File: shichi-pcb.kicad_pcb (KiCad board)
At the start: 2 copper layers, 266 x 96 mm, 168 parts, among them J1 USB_C_Receptacle_HRO_TYPE-C-3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, J2 Conn_01x04_Male, J3 Conn_01x06_Male, J4 Conn_01x04_Male, J5 Conn_01x01_Male, J6 Conn_01x01_Male, J7 Conn_01x01_Male, K1 SW_Push, K10 SW_Push, K11 SW_Push, K12 SW_Push, K13 SW_Push, K14 SW_Push, K15 SW_Push, K16 SW_Push, K17 SW_Push, K18 SW_Push, K19 SW_Push, K2 SW_Push, K20 SW_Push, K21 SW_Push, K22 SW_Push, K23 SW_Push, K24 SW_Push, K25 SW_Push, K26 SW_Push, K27 SW_Push, K28 SW_Push, K29 SW_Push, K3 SW_Push, K30 SW_Push, K31 SW_Push, K32 SW_Push, K33 SW_Push, K34 SW_Push, K35 SW_Push, K36 SW_Push, K37 SW_Push, K38 SW_Push, K39 SW_Push, K4 SW_Push, K40 SW_Push, K41 SW_Push, K42 SW_Push, K43 SW_Push, K44 SW_Push, K45 SW_Push, K46 SW_Push, K47 SW_Push, K48 SW_Push, K49 SW_Push, K5 SW_Push, K50 SW_Push, K51 SW_Push, K52 SW_Push, K53 SW_Push, K54 SW_Push, K55 SW_Push, K56 SW_Push, K57 SW_Push, K58 SW_Push, K59 SW_Push, K6 SW_Push, K60 SW_Push, K61 SW_Push, K62 SW_Push, K63 SW_Push, K64 SW_Push, K65 SW_Push, K66 SW_Push, K67 SW_Push, K68 SW_Push, K69 SW_Push, K7 SW_Push, K70 SW_Push, K71 SW_Push, K72 SW_Push, K8 SW_Push, K9 SW_Push, SW1 SW_Push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

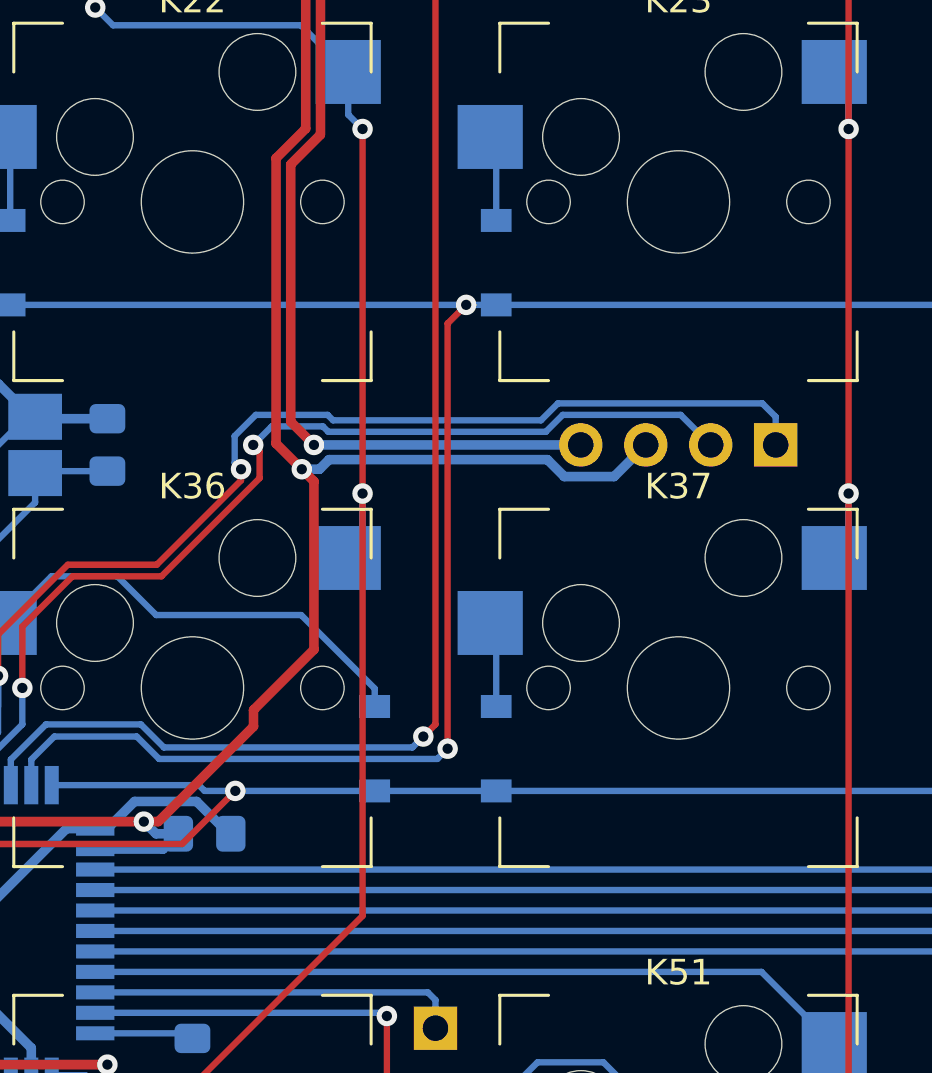
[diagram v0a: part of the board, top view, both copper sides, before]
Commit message: Add polyfuse to PCB layout design
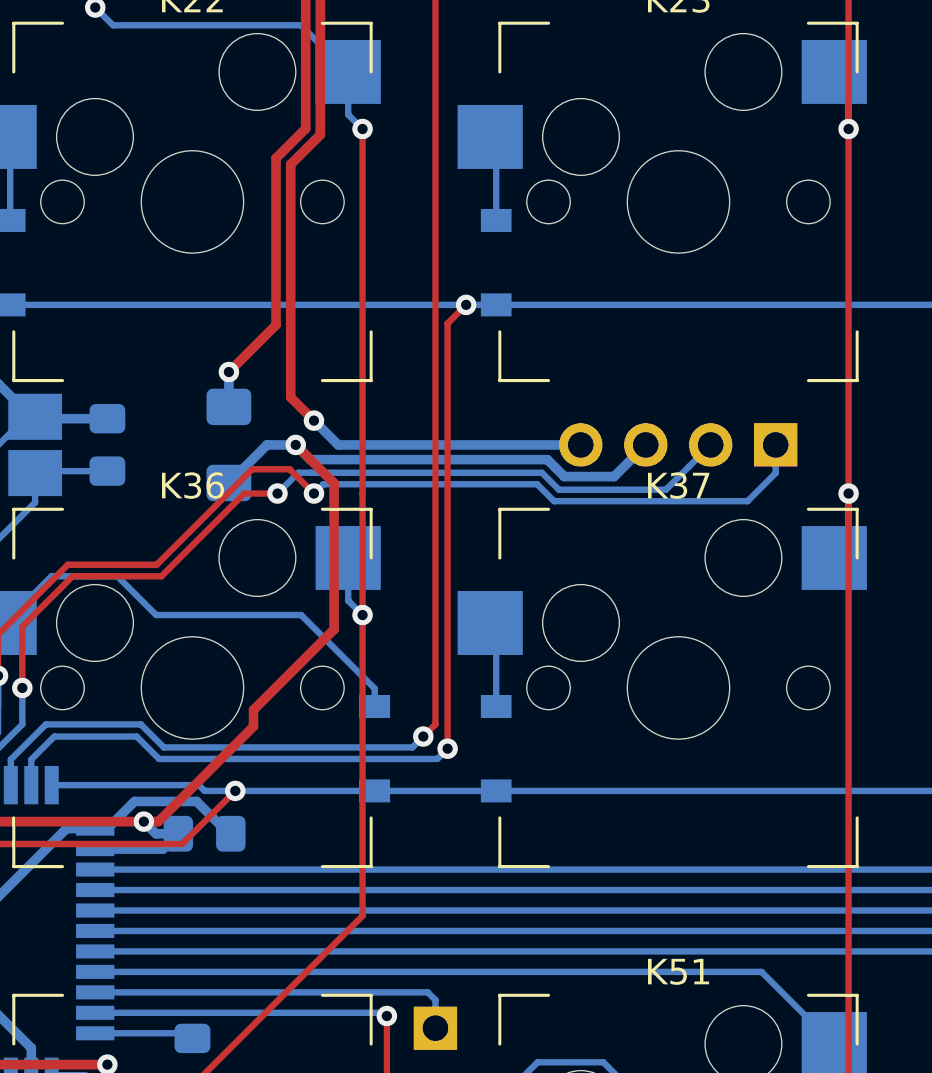
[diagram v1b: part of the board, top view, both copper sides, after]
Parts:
- added F1: Polyfuse, Fuse:Fuse_1206_3216Metric_Pad1.42x1.75mm_HandSolder, B.Cu at (193.9, 88.0)
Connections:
- C3 pad 1: VCC -> +5V
- C5 pad 1: VCC -> +5V
- C6 pad 1: VCC -> +5V
- C7 pad 1: VCC -> +5V
- C8 pad 1: VCC -> +5V
- C9 pad 1: VCC -> +5V
- J3 pad 2: VCC -> +5V
- J4 pad 3: VCC -> +5V
- R5 pad 1: VCC -> +5V
- U2 pad 14: VCC -> +5V
- U2 pad 2: VCC -> +5V
- U2 pad 24: VCC -> +5V
- U2 pad 34: VCC -> +5V
- U2 pad 44: VCC -> +5V
- U2 pad 7: VCC -> +5V
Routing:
- net +5V: track 0.00 -> 147.9 mm, vias 0 -> 8
- net VCC: track 210.7 -> 66.0 mm, vias 11 -> 4
- net SDA: track 38.8 -> 37.1 mm
- net SCL: track 44.6 -> 43.0 mm
- net GND: track 295.1 -> 294.5 mm
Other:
- board text added: "5V"

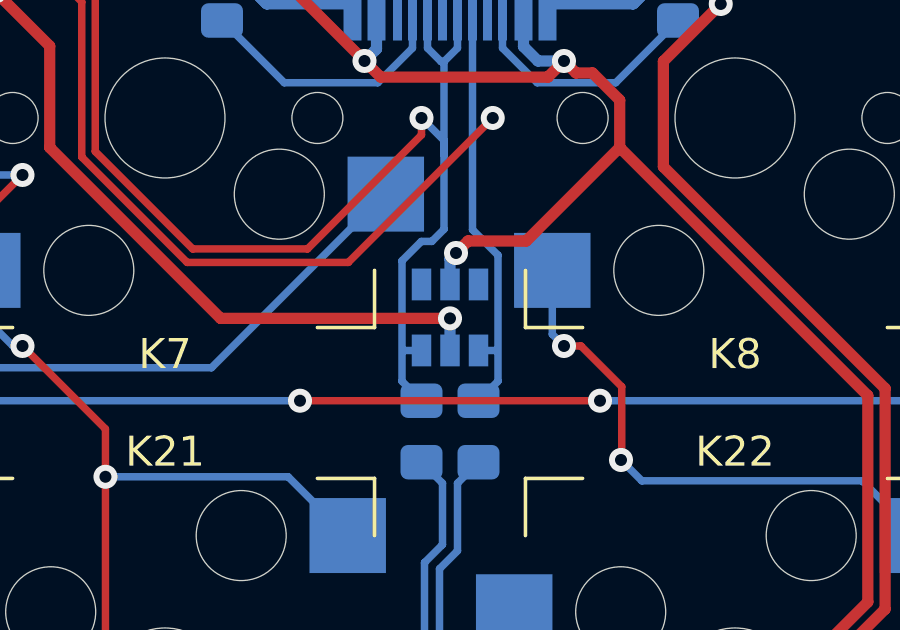
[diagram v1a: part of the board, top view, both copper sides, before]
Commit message: Update PCB layout tracks for ESD Protection
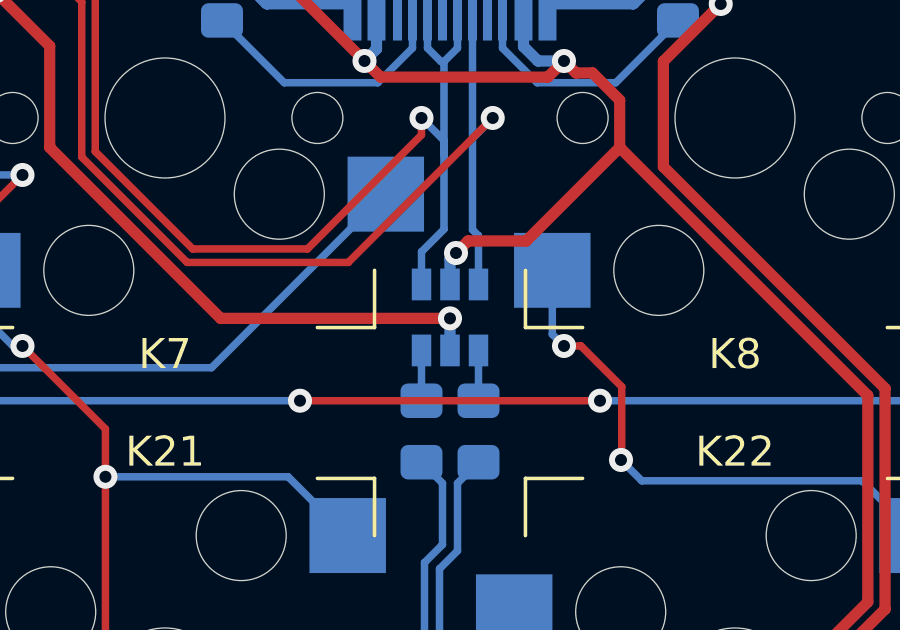
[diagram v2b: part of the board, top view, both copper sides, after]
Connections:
- J1 pad A6: Net-(J1-PadA6) -> D+Bus
- J1 pad A7: Net-(J1-PadA7) -> D-Bus
- J1 pad B6: Net-(J1-PadA6) -> D+Bus
- J1 pad B7: Net-(J1-PadA7) -> D-Bus
- J2 pad 2: Net-(J1-PadA7) -> D-Bus
- J2 pad 3: Net-(J1-PadA6) -> D+Bus
- R3 pad 1: Net-(J1-PadA7) -> Net-(R3-Pad1)
- R4 pad 1: Net-(J1-PadA6) -> Net-(R4-Pad1)
- U1 pad 1: Net-(J1-PadA6) -> Net-(R4-Pad1)
- U1 pad 3: Net-(J1-PadA7) -> Net-(R3-Pad1)
- U1 pad 4: Net-(U1-Pad4) -> D-Bus
- U1 pad 6: Net-(U1-Pad6) -> D+Bus
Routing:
- net Net-(J1-PadA6): track 47.9 -> 0.00 mm, vias 1 -> 0
- net Net-(J1-PadA7): track 43.3 -> 0.00 mm, vias 1 -> 0
- net D+Bus: track 0.00 -> 42.9 mm, vias 0 -> 1
- net D-Bus: track 0.00 -> 38.0 mm, vias 0 -> 1
- net Net-(R4-Pad1): track 0.00 -> 1.67 mm
- net Net-(R3-Pad1): track 0.00 -> 1.67 mm

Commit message: Initial arm PCB layout design
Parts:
- removed the C4 at (171.6, 106.5)
- removed J7: Conn_01x01_Male, Connector_PinHeader_2.54mm:PinHeader_1x01_P2.54mm_Vertical
- removed the R3 at (182.1, 70.0)
- removed R6: 10k, Resistor_SMD:R_0805_2012Metric_Pad1.15x1.40mm_HandSolder
- removed the U2 at (183.0, 107.0)
- removed Y1: Crystal_GND24, Crystal:Crystal_SMD_SeikoEpson_FA238-4Pin_3.2x2.5mm_HandSoldering
- added BZ1: Buzzer, Buzzer_Beeper:Buzzer_Murata_PKMCS0909E4000-R1, B.Cu at (183.0, 123.6)
- added C6: 4.7uF, Capacitor_SMD:C_0805_2012Metric_Pad1.15x1.40mm_HandSolder, B.Cu at (197.5, 88.0)
- added R5: 1k, Resistor_SMD:R_0805_2012Metric_Pad1.15x1.40mm_HandSolder, B.Cu at (175.9, 123.6)
- added SW2: SW_Push, Button_Switch_SMD:SW_SPST_TL3342, B.Cu at (201.1, 52.9)
- added U1: MCP1700-3302E_SOT23, Package_TO_SOT_SMD:SOT-23, B.Cu at (192.5, 88.0)
- added U3: STM32F072CBTx, Package_QFP:LQFP-48_7x7mm_P0.5mm, B.Cu at (183.0, 103.7)
- C1: value 22pF -> 4.7uF
- C2: value 22pF -> 0.1uF
- C3: value 10uF -> 1uF
- C4: renamed from C5; value 1uF -> 4.7uF
- F1: value Polyfuse -> 500mA
- J2, J4: footprint Connector_PinHeader_2.54mm:PinHeader_1x04_P2.54mm_Vertical -> Connector_PinSocket_2.54mm:PinSocket_1x04_P2.54mm_Vertical
- J3: footprint Connector_PinHeader_2.54mm:PinHeader_1x06_P2.54mm_Vertical -> Connector_PinSocket_2.54mm:PinSocket_1x06_P2.54mm_Vertical
- J5: value Conn_01x01_Male -> Conn_01x02_Male; footprint Connector_PinHeader_2.54mm:PinHeader_1x01_P2.54mm_Vertical -> Connector_PinSocket_2.54mm:PinSocket_1x02_P2.54mm_Vertical
- J6: footprint Connector_PinHeader_2.54mm:PinHeader_1x01_P2.54mm_Vertical -> Connector_PinSocket_2.54mm:PinSocket_1x01_P2.54mm_Vertical
- R4: value 22 -> 10k
- moved J3 57.0 mm to (221.0, 88.0)
- moved R4 41.0 mm to (203.4, 106.0), turned to 0 degrees
- moved J6 37.0 mm to (168.3, 126.0)
- moved C2 34.4 mm to (196.8, 57.6), turned to 0 degrees
- moved SW1 29.3 mm to (192.5, 52.9), turned to 0 degrees
- moved C3 29.0 mm to (195.3, 88.0), turned to 90 degrees
- moved J5 22.6 mm to (170.8, 88.0)
- moved R3 20.8 mm to (194.9, 107.5)
- moved J4 19.8 mm to (221.0, 107.0)
- moved F1 19.7 mm to (188.7, 69.0)
- moved C4 19.6 mm to (192.5, 107.5), turned to 90 degrees
- moved C8 15.9 mm to (189.4, 98.7), turned to 90 degrees
- moved C9 15.6 mm to (176.6, 99.0)
- moved D51 14.2 mm to (204.4, 118.9)
- moved C5 14.1 mm to (183.0, 111.3), turned to 0 degrees
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- renumbered C6 to C5, R5 to R3, U1 to U2
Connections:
- net /col0 renamed COL0
- net /col1 renamed COL1
- net /col10 renamed COL10
- net /col11 renamed COL11
- net /col12 renamed COL12
- net /col13 renamed COL13
- net /col2 renamed COL2
- net /col3 renamed COL3
- net /col4 renamed COL4
- net /col7 renamed COL7
- net /col8 renamed COL8
- net /col9 renamed COL9
- net /row0 renamed ROW0
- net /row1 renamed ROW1
- net /row2 renamed ROW2
- net /row3 renamed ROW3
- net /row4 renamed ROW4
- C1 pad 1: GND -> +5V
- C1 pad 2: XTAL1 -> GND
- C2 pad 1: XTAL2 -> GND
- C2 pad 2: GND -> NRST
- C3 pad 1: +5V -> +3V3
- C4 pad 1: +5V -> +3V3
- C5 pad 1: +5V -> +3V3
- C7 pad 1: +5V -> +3V3
- C8 pad 1: +5V -> +3V3
- C9 pad 1: +5V -> +3V3
- J3 pad 1: /MISO -> +3V3
- J3 pad 2: +5V -> SWDIO
- J3 pad 3: /SCK -> SWCLK
- J3 pad 4: /MOSI -> BOOT0
- J3 pad 5: RESET -> NRST
- J5 pad 1: B7 -> B14
- J6 pad 1: C6 -> AUDIO_1
- K20 pad 1: /SCK -> COL5
- K21 pad 1: /MOSI -> COL6
- K34 pad 1: /SCK -> COL5
- K35 pad 1: /MOSI -> COL6
- K48 pad 1: /SCK -> COL5
- K49 pad 1: /MOSI -> COL6
- K6 pad 1: /SCK -> COL5
- K62 pad 1: /SCK -> COL5
- K63 pad 1: /MOSI -> COL6
- K7 pad 1: /MOSI -> COL6
- K71 pad 1: /SCK -> COL5
- R3 pad 1: +5V -> NRST
- R3 pad 2: RESET -> +3V3
- R4 pad 1: Net-(R4-Pad1) -> BOOT0
- R4 pad 2: D+ -> GND
- SW1 pad 1: GND -> NRST
- SW1 pad 2: RESET -> GND
- U2 pad 1: Net-(R4-Pad1) -> D+
- U2 pad 3: Net-(R3-Pad1) -> D-
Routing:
- net +3V3: track 0.00 -> 159.7 mm, vias 0 -> 8
- net /SCK: track 134.5 -> 0.00 mm, vias 7 -> 0
- net COL5: track 0.00 -> 133.6 mm, vias 0 -> 5
- net /MOSI: track 125.0 -> 0.00 mm, vias 7 -> 0
- net NRST: track 0.00 -> 97.2 mm, vias 0 -> 5
- net COL6: track 0.00 -> 95.6 mm, vias 0 -> 6
- net BOOT0: track 0.00 -> 88.5 mm, vias 0 -> 3
- net +5V: track 147.9 -> 61.0 mm, vias 8 -> 3
- net RESET: track 80.1 -> 0.00 mm, vias 3 -> 0
- net GND: track 294.5 -> 245.8 mm, vias 6 -> 7
- net SWDIO: track 0.00 -> 46.5 mm, vias 0 -> 2
- net SWCLK: track 0.00 -> 35.2 mm
- net AUDIO_1: track 0.00 -> 33.8 mm, vias 0 -> 1
- net D-: track 59.3 -> 30.1 mm
- net D+: track 58.5 -> 30.1 mm
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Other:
- board text added: "3.3V"
- board text added: "A5"
- board text added: "B14"
- board text added: "B15"
- board text added: "BT0"
- board text added: "CLK"
- board text added: "DIO"
- board text added: "NRST"
- board text removed: "MISO"
- board text removed: "MOSI"
- board text removed: "RES"
- board text removed: "SCK"

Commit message: Remove NRST pull-up resistor
The NRST pin input driver uses the CMOS technology. It is connected to a permanent pullup resistor, RPU
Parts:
- removed the R3 at (194.9, 107.5)
- renumbered R4 to R3, R5 to R4
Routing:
- net GND: track 245.8 -> 250.2 mm, vias 7 -> 8
- net +3V3: track 159.7 -> 158.1 mm
- net NRST: track 97.2 -> 96.6 mm, vias 5 -> 3

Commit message: Add mounting holes
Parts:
- added H1: MountingHole, MountingHole:MountingHole_2.2mm_M2_Pad, F.Cu at (69.0, 69.0)
- added H2: MountingHole, MountingHole:MountingHole_2.2mm_M2_Pad, F.Cu at (69.0, 126.0)
- added H3: MountingHole, MountingHole:MountingHole_2.2mm_M2_Pad, F.Cu at (145.0, 69.0)
- added H4: MountingHole, MountingHole:MountingHole_2.2mm_M2_Pad, F.Cu at (145.0, 126.0)
- added H5: MountingHole, MountingHole:MountingHole_2.2mm_M2_Pad, F.Cu at (221.0, 69.0)
- added H6: MountingHole, MountingHole:MountingHole_2.2mm_M2_Pad, F.Cu at (221.0, 126.0)
- added H7: MountingHole, MountingHole:MountingHole_2.2mm_M2_Pad, F.Cu at (297.0, 69.0)
- added H8: MountingHole, MountingHole:MountingHole_2.2mm_M2_Pad, F.Cu at (297.0, 126.0)
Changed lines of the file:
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@@
     (tracks 1025)
     (zones 0)
-    (modules 168)
+    (modules 176)
     (nets 121)
   )
@@
     (add_net VCC)
   )
+  (module MountingHole:MountingHole_2.2mm_M2_Pad (layer F.Cu)
+    (at 297 126)
+    (descr "Mounting Hole 2.2mm, M2")
+    (tags "mounting hole 2.2mm m2")
+    (attr virtual)
+    (fp_text reference H8 (at 0 -3.2) (layer F.SilkS)
+      (effects (font (size 1 1) (thickness 0.15)))
+    )
+    (fp_text value MountingHole (at 0 3.2) (layer F.Fab)
+      (effects (font (size 1 1) (thickness 0.15)))
+    )
+    (fp_circle (center 0 0) (end 2.45 0) (layer F.CrtYd) (width 0.05))
+    (fp_circle (center 0 0) (end 2.2 0) (layer Cmts.User) (width 0.15))
+    (fp_text user %R (at 0.3 0) (layer F.Fab)
+      (effects (font (size 1 1) (thickness 0.15)))
+    )
+    (pad 1 thru_hole circle (at 0 0) (size 4.4 4.4) (drill 2.2) (layers *.Cu *.Mask))
+  )
+  (module MountingHole:MountingHole_2.2mm_M2_Pad (layer F.Cu)
+    (at 297 69)
+    (descr "Mounting Hole 2.2mm, M2")
+    (tags "mounting hole 2.2mm m2")
+    (attr virtual)
+    (fp_text reference H7 (at 0 -3.2) (layer F.SilkS)
+      (effects (font (size 1 1) (thickness 0.15)))
+    )
+    (fp_text value MountingHole (at 0 3.2) (layer F.Fab)
+      (effects (font (size 1 1) (thickness 0.15)))
+    )
+    (fp_circle (center 0 0) (end 2.45 0) (layer F.CrtYd) (width 0.05))
+    (fp_circle (center 0 0) (end 2.2 0) (layer Cmts.User) (width 0.15))
+    (fp_text user %R (at 0.3 0) (layer F.Fab)
+      (effects (font (size 1 1) (thickness 0.15)))
+    )
+    (pad 1 thru_hole circle (at 0 0) (size 4.4 4.4) (drill 2.2) (layers *.Cu *.Mask))
+  )
+  (module MountingHole:MountingHole_2.2mm_M2_Pad (layer F.Cu)
+    (at 221 126)
+    (descr "Mounting Hole 2.2mm, M2")
+    (tags "mounting hole 2.2mm m2")
+    (attr virtual)
+    (fp_text reference H6 (at 0 -3.2) (layer F.SilkS)
+      (effects (font (size 1 1) (thickness 0.15)))
+    )
+    (fp_text value MountingHole (at 0 3.2) (layer F.Fab)
+      (effects (font (size 1 1) (thickness 0.15)))
+    )
+    (fp_circle (center 0 0) (end 2.45 0) (layer F.CrtYd) (width 0.05))
+    (fp_circle (center 0 0) (end 2.2 0) (layer Cmts.User) (width 0.15))
+    (fp_text user %R (at 0.3 0) (layer F.Fab)
+      (effects (font (size 1 1) (thickness 0.15)))
+    )
+    (pad 1 thru_hole circle (at 0 0) (size 4.4 4.4) (drill 2.2) (layers *.Cu *.Mask))
+  )
+  (module MountingHole:MountingHole_2.2mm_M2_Pad (layer F.Cu)
+    (at 221 69)
+    (descr "Mounting Hole 2.2mm, M2")
+    (tags "mounting hole 2.2mm m2")
+    (attr virtual)
+    (fp_text reference H5 (at 0 -3.2) (layer F.SilkS)
+      (effects (font (size 1 1) (thickness 0.15)))
+    )
+    (fp_text value MountingHole (at 0 3.2) (layer F.Fab)
+      (effects (font (size 1 1) (thickness 0.15)))
+    )
+    (fp_circle (center 0 0) (end 2.45 0) (layer F.CrtYd) (width 0.05))
+    (fp_circle (center 0 0) (end 2.2 0) (layer Cmts.User) (width 0.15))
+    (fp_text user %R (at 0.3 0) (layer F.Fab)
+      (effects (font (size 1 1) (thickness 0.15)))
+    )
+    (pad 1 thru_hole circle (at 0 0) (size 4.4 4.4) (drill 2.2) (layers *.Cu *.Mask))
+  )
+  (module MountingHole:MountingHole_2.2mm_M2_Pad (layer F.Cu)
+    (at 145 126)
+    (descr "Mounting Hole 2.2mm, M2")
+    (tags "mounting hole 2.2mm m2")
+    (attr virtual)
+    (fp_text reference H4 (at 0 -3.2) (layer F.SilkS)
+      (effects (font (size 1 1) (thickness 0.15)))
+    )
+    (fp_text value MountingHole (at 0 3.2) (layer F.Fab)
+      (effects (font (size 1 1) (thickness 0.15)))
+    )
+    (fp_circle (center 0 0) (end 2.45 0) (layer F.CrtYd) (width 0.05))
+    (fp_circle (center 0 0) (end 2.2 0) (layer Cmts.User) (width 0.15))
+    (fp_text user %R (at 0.3 0) (layer F.Fab)
+      (effects (font (size 1 1) (thickness 0.15)))
+    )
+    (pad 1 thru_hole circle (at 0 0) (size 4.4 4.4) (drill 2.2) (layers *.Cu *.Mask))
+  )
+  (module MountingHole:MountingHole_2.2mm_M2_Pad (layer F.Cu)
+    (at 145 69)
+    (descr "Mounting Hole 2.2mm, M2")
+    (tags "mounting hole 2.2mm m2")
+    (attr virtual)
+    (fp_text reference H3 (at 0 -3.2) (layer F.SilkS)
+      (effects (font (size 1 1) (thickness 0.15)))
+    )
+    (fp_text value MountingHole (at 0 3.2) (layer F.Fab)
+      (effects (font (size 1 1) (thickness 0.15)))
+    )
+    (fp_circle (center 0 0) (end 2.45 0) (layer F.CrtYd) (width 0.05))
+    (fp_circle (center 0 0) (end 2.2 0) (layer Cmts.User) (width 0.15))
+    (fp_text user %R (at 0.3 0) (layer F.Fab)
+      (effects (font (size 1 1) (thickness 0.15)))
+    )
+    (pad 1 thru_hole circle (at 0 0) (size 4.4 4.4) (drill 2.2) (layers *.Cu *.Mask))
+  )
+  (module MountingHole:MountingHole_2.2mm_M2_Pad (layer F.Cu)
+    (at 69 126)
+    (descr "Mounting Hole 2.2mm, M2")
+    (tags "mounting hole 2.2mm m2")
+    (attr virtual)
+    (fp_text reference H2 (at 0 -3.2) (layer F.SilkS)
+      (effects (font (size 1 1) (thickness 0.15)))
+    )
+    (fp_text value MountingHole (at 0 3.2) (layer F.Fab)
+      (effects (font (size 1 1) (thickness 0.15)))
+    )
+    (fp_circle (center 0 0) (end 2.45 0) (layer F.CrtYd) (width 0.05))
+    (fp_circle (center 0 0) (end 2.2 0) (layer Cmts.User) (width 0.15))
+    (fp_text user %R (at 0.3 0) (layer F.Fab)
+      (effects (font (size 1 1) (thickness 0.15)))
+    )
+    (pad 1 thru_hole circle (at 0 0) (size 4.4 4.4) (drill 2.2) (layers *.Cu *.Mask))
+  )
+  (module MountingHole:MountingHole_2.2mm_M2_Pad (layer F.Cu)
+    (at 69 69)
+    (descr "Mounting Hole 2.2mm, M2")
+    (tags "mounting hole 2.2mm m2")
+    (attr virtual)
+    (fp_text reference H1 (at 0 -3.2) (layer F.SilkS)
+      (effects (font (size 1 1) (thickness 0.15)))
+    )
+    (fp_text value MountingHole (at 0 3.2) (layer F.Fab)
+      (effects (font (size 1 1) (thickness 0.15)))
+    )
+    (fp_circle (center 0 0) (end 2.45 0) (layer F.CrtYd) (width 0.05))
+    (fp_circle (center 0 0) (end 2.2 0) (layer Cmts.User) (width 0.15))
+    (fp_text user %R (at 0.3 0) (layer F.Fab)
+      (effects (font (size 1 1) (thickness 0.15)))
+    )
+    (pad 1 thru_hole circle (at 0 0) (size 4.4 4.4) (drill 2.2) (layers *.Cu *.Mask))
+  )
   (module Package_TO_SOT_SMD:SOT-23 (layer B.Cu)
